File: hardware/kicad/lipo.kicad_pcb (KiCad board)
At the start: 2 copper layers, 70 x 50 mm, 59 parts

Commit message: hardware: UART debug header on all boards, I2C header and rail test pads on carrier, SDA/SCL pads on pack
Header is 1x3 2.54 mm (GND, MCU TX, MCU RX), hand-soldered, kept out of the BOM.
Carrier uses Heltec UART0 (GPIO43/44), STM32 boards USART1 (PA9/PA10).

Co-Authored-By: Claude Sonnet 5.5 <noreply@anthropic.com>
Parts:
- added J_UART1: UART, Connector_PinHeader_2.54mm:PinHeader_1x03_P2.54mm_Vertical, F.Cu at (29.3, 40.5)
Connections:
- U_MCU pad 19: unconnected-(U_MCU-PA9-Pad19) -> UART_TX
- U_MCU pad 21: unconnected-(U_MCU-PA10-Pad21) -> UART_RX
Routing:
- net GND: track 292.5 -> 272.1 mm, vias 2 -> 5
- net SW_A: track 18.0 -> 25.9 mm
- net UART_TX: track 0.00 -> 6.57 mm, vias 0 -> 1
- net BOOT_B: track 14.5 -> 8.70 mm, vias 2 -> 0
- net SCL_EXT: track 55.3 -> 60.2 mm
- net VBAT_SW: track 43.0 -> 47.2 mm, vias 3 -> 2
- net UART_RX: track 0.00 -> 3.98 mm
- net TAP2_ADC: track 48.4 -> 44.6 mm
- net NRST: track 22.9 -> 19.1 mm
- net BOOT0: track 28.2 -> 24.5 mm
- net FB_A: track 9.24 -> 12.2 mm
- net SW_B: track 21.4 -> 19.3 mm
- net SDA_EXT: track 54.7 -> 56.5 mm
- net TAP1_ADC: track 51.1 -> 49.5 mm
- net +3V3: track 37.7 -> 36.2 mm, vias 4 -> 5
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
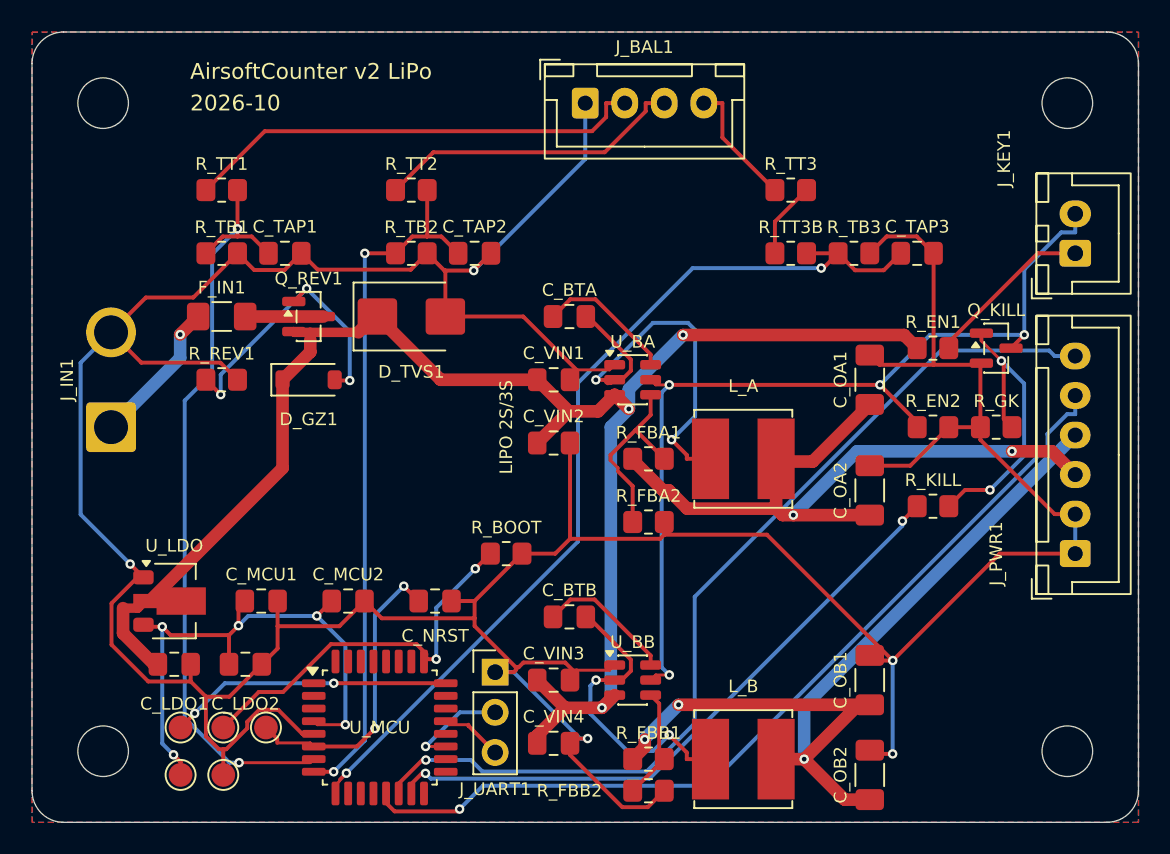
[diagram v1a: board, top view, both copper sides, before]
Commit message: hardware: KiCad 10 pipeline fixes, +5V reservoir caps, NS4168 1uF, pack UART header off the holders
KiCad 9 -> 10.0.7 broke the generators even on HEAD:
- gen_sch: libraries moved (hide yes) from effects to the property; read both,
  write it back into effects (KiCad 9 format), so hidden fields stop showing
  on every sheet and stop blocking the schematic router. Add the title block.
- gen_pcb: SetDoNotAllowCopperPour -> SetDoNotAllowZoneFills; copy the symbol's
  Datasheet/Description/Sim fields onto footprints (schematic parity now fails
  DRC); refuse THT pads under bottom-side parts (PTH_UNDER_OK allowlist).
- route.py: Power class routed at +40 um (Freerouting's octagons undercut 0.8 mm
  round ends, KiCad 10 exports no clearance margin), falling back to no margin
  if that leaves a connection unrouted; strip dangling stubs after SES import.
- pack: USB-C shield pin S1 -> SH; pack_tme: VSSOP-10 -> MSOP-10 footprint.

Design changes from the Konnect MCP review and datasheet check:
- carrier: C_5V1 10 uF + C_5V2 100 nF on +5V at J_PWR1 (no local cap before);
  C_AMP2 100 nF -> 1 uF per NS4168 datasheet (100 uF || 1 uF). carrier_tme
  places the new caps clear of its DAC.
- pack/pack_tme: J_UART1 sat under BT4 (bottom-side 18650 holder), caught by
  KiCad 10's pth_inside_courtyard; moved to the right strip, label in pin order.
  The NTC beads stay in the holder window (check ignored, gen_pcb enforces it).
- Docs: ORDERING counts, NS4168/TCA9534/BSS138/1N4148W datasheet check,
  TCA9534 P6/P7 firmware note.

All six boards: ERC 0, DRC 0 (0 unconnected, 0 parity), gerbers ok.

Co-Authored-By: Claude Opus 5.5 <noreply@anthropic.com>
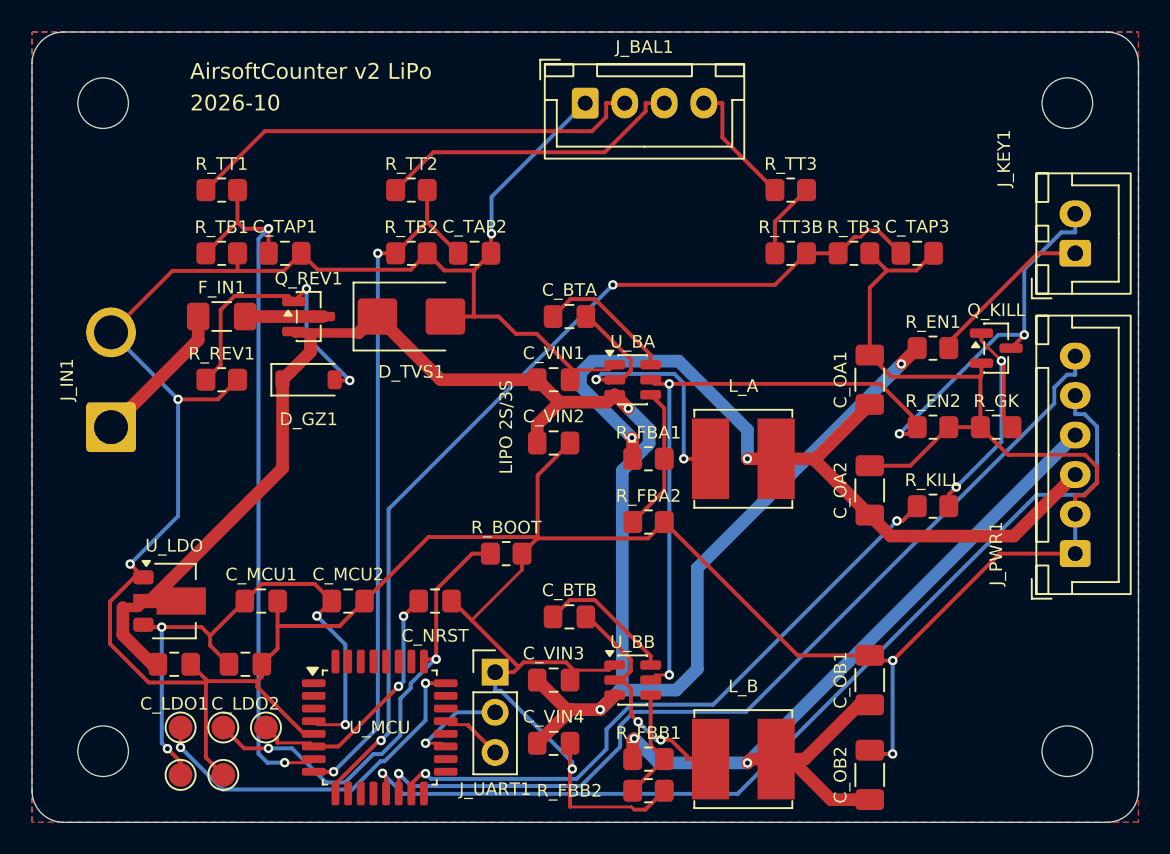
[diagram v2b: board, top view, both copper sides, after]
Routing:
- net VIN: track 105.2 -> 116.7 mm
- net SW_A: track 25.9 -> 19.7 mm
- net SWDIO: track 17.9 -> 23.3 mm
- net SDA_EXT: track 56.5 -> 61.7 mm
- net BOOT0: track 24.5 -> 29.3 mm
- net SW_B: track 19.3 -> 14.9 mm
- net TAP1_ADC: track 49.5 -> 45.8 mm
- net VBAT_SW: track 47.2 -> 50.6 mm
- net FB_A: track 12.2 -> 9.24 mm
- net +5V: track 56.5 -> 53.8 mm, vias 3 -> 2
- net NRST: track 19.1 -> 16.5 mm
- net SCL_EXT: track 60.2 -> 57.7 mm
- net GND: track 272.1 -> 274.5 mm, vias 5 -> 6
- net KILL_G: track 19.4 -> 17.3 mm
- net BUCK_EN: track 59.5 -> 60.6 mm
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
